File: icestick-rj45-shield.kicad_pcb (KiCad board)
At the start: 2 copper layers, 56.4 x 67.1 mm, 22 parts, among them J1 Conn_01x10, J2 Conn_01x10, U1 Si8640BB-B-IS1, U2 REG71050, U3 Si8640BB-B-IS1, U4 Si8640BB-B-IS1, U5 Si8640BB-B-IS1

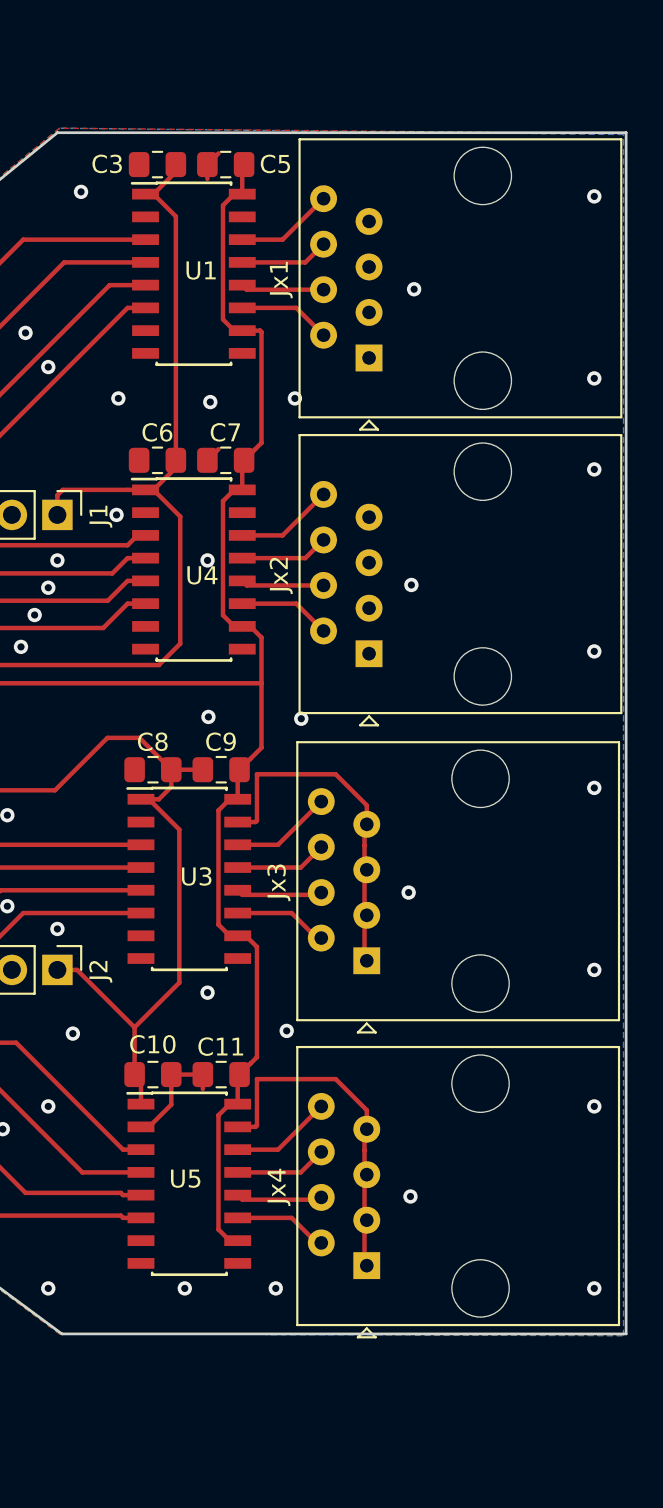
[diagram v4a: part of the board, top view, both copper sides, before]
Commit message: Switched to Si8660 isolator and changed RJ-45 connector
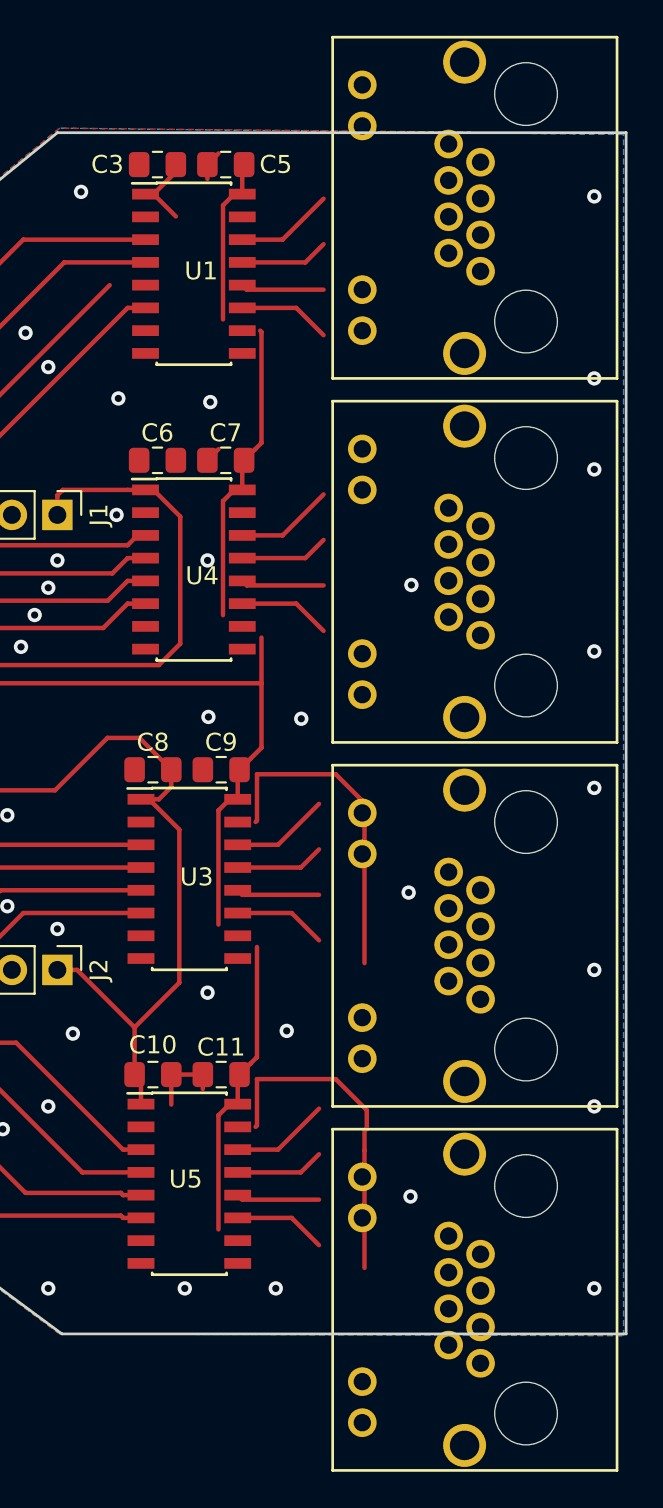
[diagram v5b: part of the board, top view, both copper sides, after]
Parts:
- removed Jx1, Jx2, Jx3, Jx4: RJ45, Connector_RJ:RJ45_Amphenol_54602-x08_Horizontal
- added J3: TE-Connectivity-406549-6, Matthias:TE-Connectivity-406549-6, B.Cu at (167.6, 73.7)
- added J4: TE-Connectivity-406549-6, Matthias:TE-Connectivity-406549-6, B.Cu at (167.6, 94.0)
- added J5: TE-Connectivity-406549-6, Matthias:TE-Connectivity-406549-6, B.Cu at (167.6, 114.3)
- added J6: TE-Connectivity-406549-6, Matthias:TE-Connectivity-406549-6, B.Cu at (167.6, 134.6)
- U1, U3, U4, U5: value Si8640BB-B-IS1 -> Si8660
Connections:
- U1 pad 10: +5V -> (no net)
- U1 pad 15: GND -> (no net)
- U1 pad 2: GND -> (no net)
- U3 pad 10: +5V -> (no net)
- U3 pad 15: GND -> (no net)
- U3 pad 2: GND -> (no net)
- U4 pad 10: +5V -> (no net)
- U4 pad 15: GND -> (no net)
- U4 pad 2: GND -> (no net)
- U5 pad 10: +5V -> (no net)
- U5 pad 15: GND -> (no net)
- U5 pad 2: GND -> (no net)
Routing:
- net GND: track 57.7 -> 24.1 mm, vias 52 -> 50
- net (no net): track 0.00 -> 25.8 mm
- net +3V3: track 122.9 -> 107.1 mm
- net +5V: track 97.8 -> 88.8 mm
- net /iCEstick connector/FPGA_117: track 28.0 -> 26.0 mm

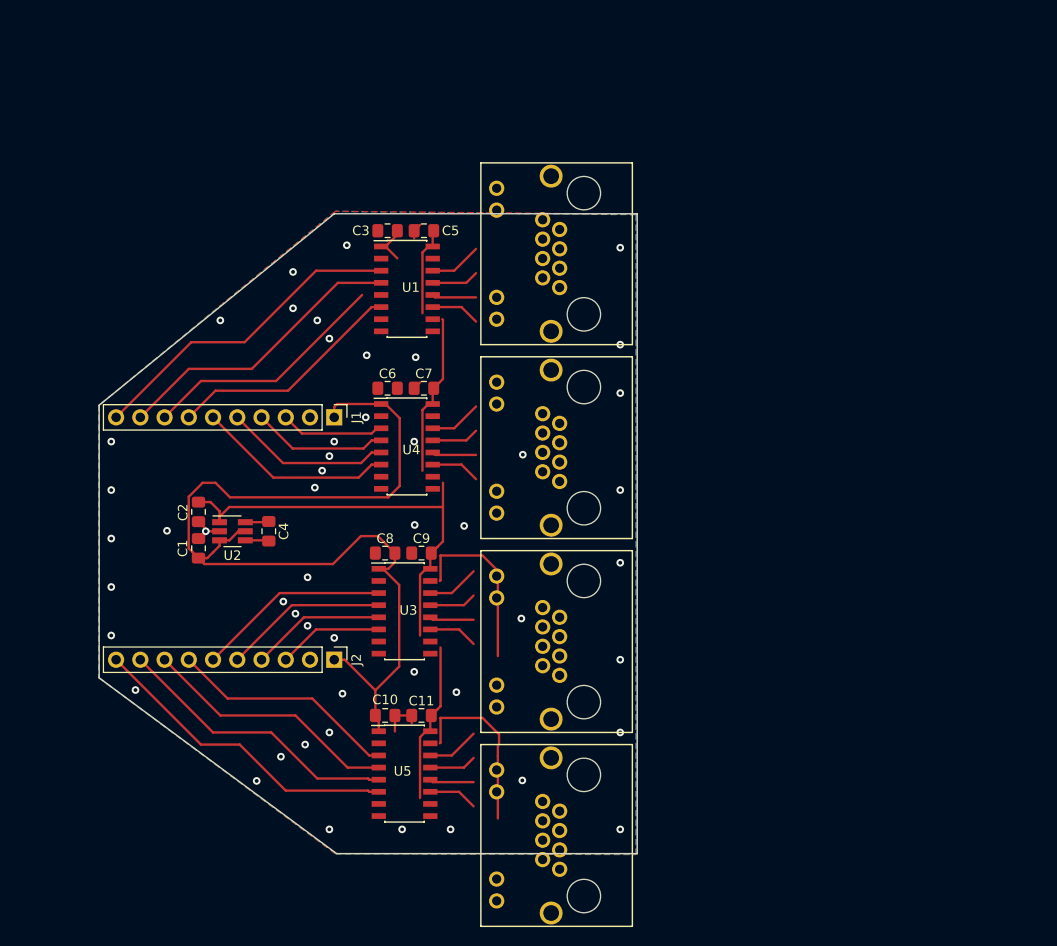
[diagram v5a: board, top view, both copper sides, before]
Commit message: Began redesigning with Si8660
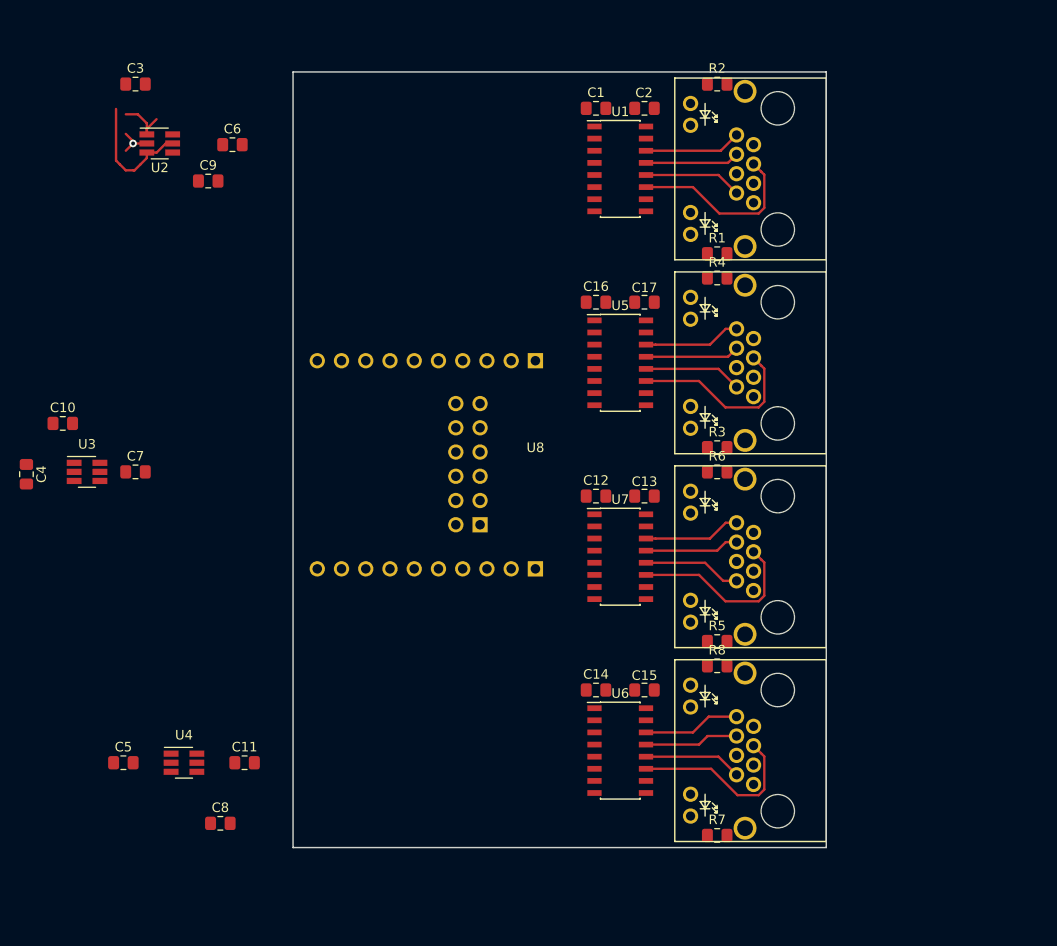
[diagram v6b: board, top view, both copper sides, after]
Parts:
- removed J5, J6: TE-Connectivity-406549-6, Matthias:TE-Connectivity-406549-6
- added C12: 220nF, Capacitor_SMD:C_0805_2012Metric_Pad1.15x1.40mm_HandSolder, F.Cu at (168.9, 99.1)
- added C13: 220nF, Capacitor_SMD:C_0805_2012Metric_Pad1.15x1.40mm_HandSolder, F.Cu at (174.0, 99.1)
- added C14: 220nF, Capacitor_SMD:C_0805_2012Metric_Pad1.15x1.40mm_HandSolder, F.Cu at (168.9, 119.4)
- added C15: 220nF, Capacitor_SMD:C_0805_2012Metric_Pad1.15x1.40mm_HandSolder, F.Cu at (174.0, 119.4)
- added C16: 220nF, Capacitor_SMD:C_0805_2012Metric_Pad1.15x1.40mm_HandSolder, F.Cu at (168.9, 78.7)
- added C17: 220nF, Capacitor_SMD:C_0805_2012Metric_Pad1.15x1.40mm_HandSolder, F.Cu at (174.0, 78.7)
- added R1: 470R, Resistor_SMD:R_0805_2012Metric_Pad1.15x1.40mm_HandSolder, F.Cu at (181.6, 73.7)
- added R2: 470R, Resistor_SMD:R_0805_2012Metric_Pad1.15x1.40mm_HandSolder, F.Cu at (181.6, 55.9)
- added R3: 470R, Resistor_SMD:R_0805_2012Metric_Pad1.15x1.40mm_HandSolder, F.Cu at (181.6, 94.0)
- added R4: 470R, Resistor_SMD:R_0805_2012Metric_Pad1.15x1.40mm_HandSolder, F.Cu at (181.6, 76.2)
- added R5: 470R, Resistor_SMD:R_0805_2012Metric_Pad1.15x1.40mm_HandSolder, F.Cu at (181.6, 114.3)
- added R6: 470R, Resistor_SMD:R_0805_2012Metric_Pad1.15x1.40mm_HandSolder, F.Cu at (181.6, 96.5)
- added R7: 470R, Resistor_SMD:R_0805_2012Metric_Pad1.15x1.40mm_HandSolder, F.Cu at (181.6, 134.6)
- added R8: 470R, Resistor_SMD:R_0805_2012Metric_Pad1.15x1.40mm_HandSolder, F.Cu at (181.6, 116.8)
- added U6: Si8660, Package_SO:SOIC-16_3.9x9.9mm_P1.27mm, F.Cu at (171.4, 125.7)
- added U7: Si8660, Package_SO:SOIC-16_3.9x9.9mm_P1.27mm, F.Cu at (171.4, 105.4)
- added U8: iCEstick, Matthias:iCEstick, F.Cu at (162.6, 106.7)
- C10, C11, C3, C4, C5, C6, C7, C8, C9: value 220nF -> 2.2uF
- J1, J2: value Conn_01x10 -> TE-Connectivity-406549-6; footprint Connector_PinHeader_2.54mm:PinHeader_1x10_P2.54mm_Vertical -> Matthias:TE-Connectivity-406549-6; moved to B.Cu
- U3, U4: value Si8660 -> REG71050; footprint Package_SO:SOIC-16_3.9x9.9mm_P1.27mm -> Package_TO_SOT_SMD:SOT-23-6_Handsoldering
- moved C5 64.0 mm to (119.4, 127.0), turned to 0 degrees
- moved C2 63.0 mm to (174.0, 58.4), turned to 180 degrees
- moved C1 62.1 mm to (168.9, 58.4), turned to 0 degrees
- moved J2 55.9 mm to (188.0, 85.1)
- moved J1 53.3 mm to (188.0, 64.8)
- moved U5 48.6 mm to (171.4, 85.1)
- moved C10 45.6 mm to (113.0, 91.4)
- moved C9 44.9 mm to (128.3, 66.0), turned to 0 degrees
- moved U2 41.3 mm to (123.2, 62.1)
- moved U4 40.6 mm to (125.7, 127.0)
- moved J3 37.7 mm to (188.0, 105.4)
- moved J4 37.7 mm to (188.0, 125.7)
- moved U3 36.3 mm to (115.6, 96.5)
- moved C8 33.2 mm to (129.5, 133.3), turned to 0 degrees
- moved C7 31.5 mm to (120.7, 96.5), turned to 0 degrees
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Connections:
- C10 pad 1: +3V3 -> +5V
- C4 pad 1: Net-(C4-Pad1) -> +3V3
- C4 pad 2: Net-(C4-Pad2) -> GND
- C5 pad 1: +5V -> +3V3
- C6 pad 1: +3V3 -> Net-(C6-Pad1)
- C6 pad 2: GND -> Net-(C6-Pad2)
- C7 pad 1: +5V -> Net-(C7-Pad1)
- C7 pad 2: GND -> Net-(C7-Pad2)
- C8 pad 1: +3V3 -> Net-(C8-Pad1)
- C8 pad 2: GND -> Net-(C8-Pad2)
- J1 pad 1: +3V3 -> GND
- J1 pad 10: /iCEstick connector/FPGA_119 -> /Connector 1/LED1
- J1 pad 2: GND -> /Isolator 1/Out3
- J1 pad 3: /iCEstick connector/FPGA_112 -> GND
- J1 pad 4: /iCEstick connector/FPGA_113 -> GND
- J1 pad 5: /iCEstick connector/FPGA_114 -> /Isolator 1/Out4
- J1 pad 6: /iCEstick connector/FPGA_115 -> /Isolator 1/Out2
- J1 pad 7: /iCEstick connector/FPGA_116 -> GND
- J1 pad 8: /iCEstick connector/FPGA_117 -> /Isolator 1/Out1
- J1 pad 9: /iCEstick connector/FPGA_118 -> Net-(J1-Pad9)
- J2 pad 1: +3V3 -> GND
- J2 pad 10: /iCEstick connector/FPGA_44 -> /Connector 2/LED1
- J2 pad 2: GND -> /Isolator 2/Out3
- J2 pad 3: /iCEstick connector/FPGA_62 -> GND
- J2 pad 4: /iCEstick connector/FPGA_61 -> GND
- J2 pad 5: /iCEstick connector/FPGA_60 -> /Isolator 2/Out4
- J2 pad 6: /iCEstick connector/FPGA_56 -> /Isolator 2/Out2
- J2 pad 7: /iCEstick connector/FPGA_48 -> GND
- J2 pad 8: /iCEstick connector/FPGA_47 -> /Isolator 2/Out1
- J2 pad 9: /iCEstick connector/FPGA_45 -> Net-(J2-Pad9)
- J3 pad 1: /Connector 1/OUT1 -> GND
- J3 pad 10: (no net) -> /Connector 3/LED1
- J3 pad 11: (no net) -> Net-(J3-Pad11)
- J3 pad 12: (no net) -> /Connector 3/LED2
- J3 pad 2: GND -> /Isolator 3/Out3
- J3 pad 3: /Connector 1/OUT2 -> GND
- J3 pad 5: /Connector 1/OUT3 -> /Isolator 3/Out4
- J3 pad 6: GND -> /Isolator 3/Out2
- J3 pad 7: /Connector 1/OUT4 -> GND
- J3 pad 8: GND -> /Isolator 3/Out1
- J3 pad 9: (no net) -> Net-(J3-Pad9)
- J4 pad 1: /Connector 2/OUT1 -> GND
- J4 pad 10: (no net) -> /Connector 4/LED1
- J4 pad 11: (no net) -> Net-(J4-Pad11)
- J4 pad 12: (no net) -> /Connector 4/LED2
- J4 pad 2: GND -> /Isolator 4/Out3
- J4 pad 3: /Connector 2/OUT2 -> GND
- J4 pad 5: /Connector 2/OUT3 -> /Isolator 4/Out4
- J4 pad 6: GND -> /Isolator 4/Out2
- J4 pad 7: /Connector 2/OUT4 -> GND
- J4 pad 8: GND -> /Isolator 4/Out1
- J4 pad 9: (no net) -> Net-(J4-Pad9)
- U1 pad 10: (no net) -> /Connector 1/LED1
- U1 pad 11: /Connector 1/OUT4 -> /Isolator 1/Out4
- U1 pad 12: /Connector 1/OUT3 -> /Isolator 1/Out3
- U1 pad 13: /Connector 1/OUT2 -> /Isolator 1/Out2
- U1 pad 14: /Connector 1/OUT1 -> /Isolator 1/Out1
- U1 pad 15: (no net) -> /Connector 1/LED2
- U1 pad 2: (no net) -> /iCEstick connector/FPGA_78
- U1 pad 7: (no net) -> /iCEstick connector/FPGA_79
- U2 pad 4: Net-(C4-Pad1) -> Net-(C6-Pad1)
- U2 pad 6: Net-(C4-Pad2) -> Net-(C6-Pad2)
- U3 pad 1: +3V3 -> +5V
- U3 pad 2: (no net) -> GND
- U3 pad 3: /iCEstick connector/FPGA_56 -> +3V3
- U3 pad 4: /iCEstick connector/FPGA_60 -> Net-(C7-Pad1)
- U3 pad 5: /iCEstick connector/FPGA_61 -> +3V3
- U3 pad 6: /iCEstick connector/FPGA_62 -> Net-(C7-Pad2)
- U4 pad 1: +3V3 -> +5V
- U4 pad 2: (no net) -> GND
- U4 pad 3: /iCEstick connector/FPGA_112 -> +3V3
- U4 pad 4: /iCEstick connector/FPGA_113 -> Net-(C8-Pad1)
- U4 pad 5: /iCEstick connector/FPGA_114 -> +3V3
- U4 pad 6: /iCEstick connector/FPGA_115 -> Net-(C8-Pad2)
- U5 pad 10: (no net) -> /Connector 2/LED1
- U5 pad 11: /Connector 4/OUT4 -> /Isolator 2/Out4
- U5 pad 12: /Connector 4/OUT3 -> /Isolator 2/Out3
- U5 pad 13: /Connector 4/OUT2 -> /Isolator 2/Out2
- U5 pad 14: /Connector 4/OUT1 -> /Isolator 2/Out1
- U5 pad 15: (no net) -> /Connector 2/LED2
- U5 pad 2: (no net) -> /iCEstick connector/FPGA_80
- U5 pad 3: /iCEstick connector/FPGA_48 -> /iCEstick connector/FPGA_112
- U5 pad 4: /iCEstick connector/FPGA_47 -> /iCEstick connector/FPGA_113
- U5 pad 5: /iCEstick connector/FPGA_45 -> /iCEstick connector/FPGA_114
- U5 pad 6: /iCEstick connector/FPGA_44 -> /iCEstick connector/FPGA_115
- U5 pad 7: (no net) -> /iCEstick connector/FPGA_81
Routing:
- net +3V3: track 107.1 -> 13.3 mm
- net +5V: track 88.8 -> 5.77 mm
- net /iCEstick connector/FPGA_119: track 34.1 -> 0.00 mm
- net /iCEstick connector/FPGA_44: track 33.3 -> 0.00 mm
- net /iCEstick connector/FPGA_118: track 31.1 -> 0.00 mm
- net /iCEstick connector/FPGA_45: track 30.2 -> 0.00 mm
- net /iCEstick connector/FPGA_47: track 27.1 -> 0.00 mm
- net /iCEstick connector/FPGA_117: track 26.0 -> 0.00 mm
- net (no net): track 25.8 -> 0.00 mm
- net /iCEstick connector/FPGA_116: track 24.9 -> 0.00 mm
- net /iCEstick connector/FPGA_48: track 24.1 -> 0.00 mm
- net /iCEstick connector/FPGA_115: track 20.8 -> 0.00 mm
- net /iCEstick connector/FPGA_56: track 20.3 -> 0.00 mm
- net GND: track 24.1 -> 3.84 mm, vias 50 -> 1
- net /Isolator 3/Out4: track 0.00 -> 18.8 mm
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- removed copper zone on B.Cu, net GND
- removed copper zone on F.Cu, net GND
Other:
- board size 56.4 x 67.1 mm -> 55.9 x 81.3 mm

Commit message: Finished layout with 4x Si8660
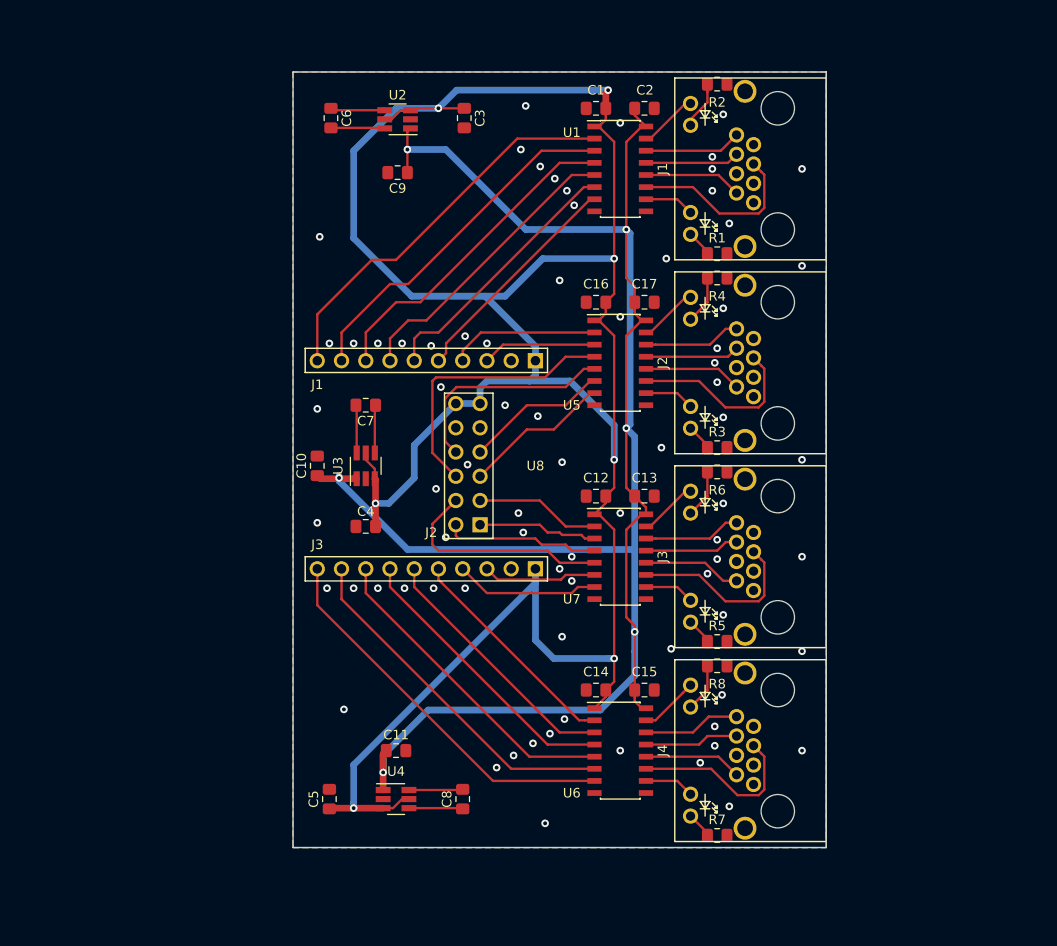
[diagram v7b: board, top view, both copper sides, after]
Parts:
- moved C4 36.0 mm to (144.8, 102.2), turned to 180 degrees
- moved C3 34.6 mm to (155.1, 59.4), turned to 270 degrees
- moved U3 29.2 mm to (144.8, 95.9), turned to 90 degrees
- moved C10 27.0 mm to (139.7, 95.9), turned to 90 degrees
- moved C8 25.5 mm to (154.9, 130.8), turned to 90 degrees
- moved C7 25.1 mm to (144.8, 89.5), turned to 180 degrees
- moved U2 25.1 mm to (148.1, 59.6), turned to 180 degrees
- moved U4 22.5 mm to (148.0, 130.8)
- moved C5 21.9 mm to (141.0, 130.8), turned to 90 degrees
- moved C9 19.9 mm to (148.1, 65.2), turned to 180 degrees
- moved C11 15.9 mm to (148.0, 125.7)
- moved C6 10.7 mm to (141.1, 59.4), turned to 270 degrees
- turned C1 to 180 degrees
- turned C12 to 180 degrees
- turned C13 to 0 degrees
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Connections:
- U1 pad 2: /iCEstick connector/FPGA_78 -> /iCEstick connector/FPGA_119
- U1 pad 3: /iCEstick connector/FPGA_119 -> /iCEstick connector/FPGA_118
- U1 pad 4: /iCEstick connector/FPGA_118 -> /iCEstick connector/FPGA_117
- U1 pad 5: /iCEstick connector/FPGA_117 -> /iCEstick connector/FPGA_116
- U1 pad 6: /iCEstick connector/FPGA_116 -> /iCEstick connector/FPGA_115
- U1 pad 7: /iCEstick connector/FPGA_79 -> /iCEstick connector/FPGA_114
- U5 pad 2: /iCEstick connector/FPGA_80 -> /iCEstick connector/FPGA_113
- U5 pad 4: /iCEstick connector/FPGA_113 -> /iCEstick connector/FPGA_90
- U5 pad 5: /iCEstick connector/FPGA_114 -> /iCEstick connector/FPGA_91
- U5 pad 6: /iCEstick connector/FPGA_115 -> /iCEstick connector/FPGA_81
- U5 pad 7: /iCEstick connector/FPGA_81 -> /iCEstick connector/FPGA_80
- U6 pad 2: /iCEstick connector/FPGA_90 -> /iCEstick connector/FPGA_60
- U6 pad 3: /iCEstick connector/FPGA_48 -> /iCEstick connector/FPGA_56
- U6 pad 4: /iCEstick connector/FPGA_47 -> /iCEstick connector/FPGA_48
- U6 pad 5: /iCEstick connector/FPGA_45 -> /iCEstick connector/FPGA_47
- U6 pad 6: /iCEstick connector/FPGA_44 -> /iCEstick connector/FPGA_45
- U6 pad 7: /iCEstick connector/FPGA_91 -> /iCEstick connector/FPGA_44
- U7 pad 2: /iCEstick connector/FPGA_87 -> /iCEstick connector/FPGA_79
- U7 pad 3: /iCEstick connector/FPGA_56 -> /iCEstick connector/FPGA_78
- U7 pad 4: /iCEstick connector/FPGA_60 -> /iCEstick connector/FPGA_87
- U7 pad 5: /iCEstick connector/FPGA_61 -> /iCEstick connector/FPGA_88
- U7 pad 7: /iCEstick connector/FPGA_88 -> /iCEstick connector/FPGA_61
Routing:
- net +3V3: track 13.3 -> 264.7 mm, vias 0 -> 7
- net +5V: track 5.77 -> 223.1 mm, vias 0 -> 6
- net /iCEstick connector/FPGA_119: track 0.00 -> 42.0 mm
- net /iCEstick connector/FPGA_44: track 0.00 -> 40.5 mm
- net /iCEstick connector/FPGA_118: track 0.00 -> 37.4 mm
- net /iCEstick connector/FPGA_45: track 0.00 -> 37.0 mm
- net /iCEstick connector/FPGA_117: track 0.00 -> 34.3 mm
- net /iCEstick connector/FPGA_47: track 0.00 -> 33.6 mm
- net /iCEstick connector/FPGA_116: track 0.00 -> 30.9 mm
- net /iCEstick connector/FPGA_48: track 0.00 -> 30.2 mm
- net /iCEstick connector/FPGA_90: track 0.00 -> 29.0 mm
- net /iCEstick connector/FPGA_115: track 0.00 -> 27.8 mm
- net /iCEstick connector/FPGA_56: track 0.00 -> 27.1 mm
- net /iCEstick connector/FPGA_114: track 0.00 -> 24.0 mm
- net /iCEstick connector/FPGA_60: track 0.00 -> 23.6 mm
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- added copper zone on B.Cu, net GND
- added copper zone on F.Cu, net GND
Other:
- net class Power added: clearance 0.2, trace_width 0.7, via_dia 0.8, via_drill 0.4
